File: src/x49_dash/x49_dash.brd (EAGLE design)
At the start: 171.4 x 95.2 mm, 63 parts, among them J1 1-776276-1, Q1 BSS138, U2 MCP2562

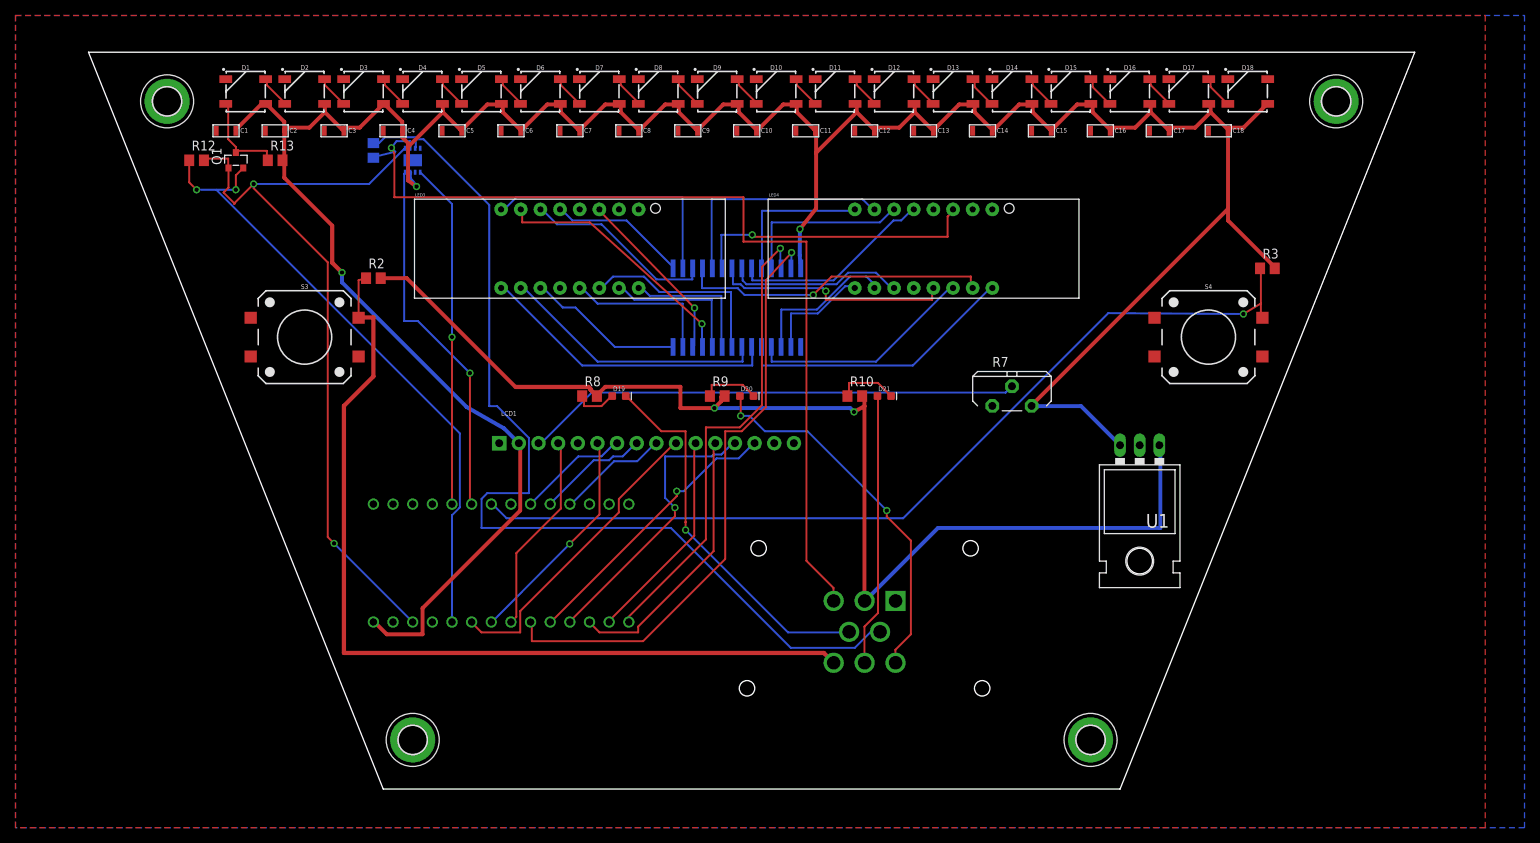
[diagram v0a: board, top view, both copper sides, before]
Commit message: x49_dash: WIP Move teensy parts closer together, clean up routing
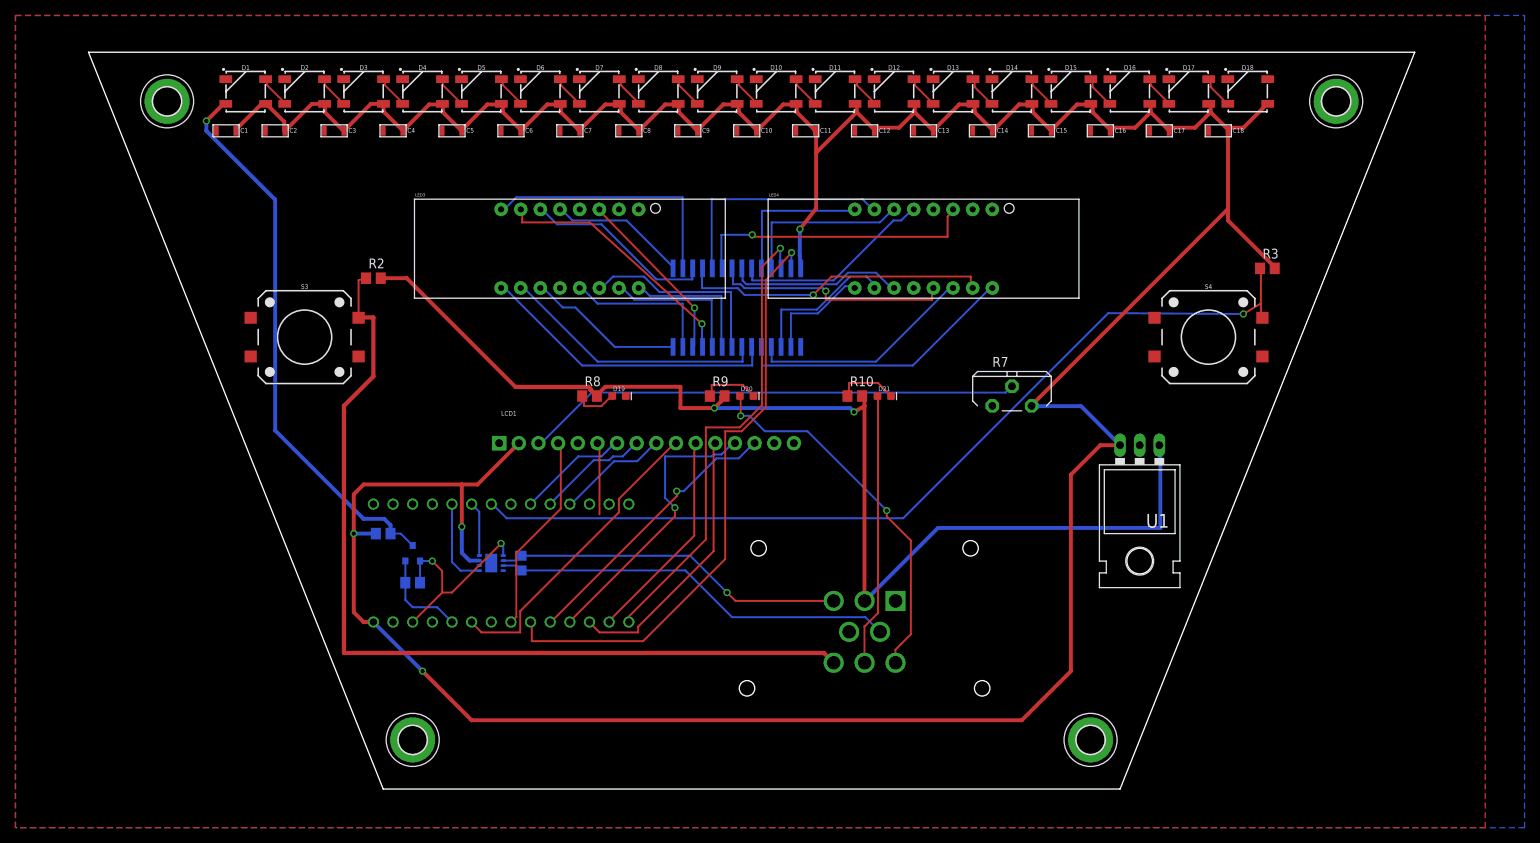
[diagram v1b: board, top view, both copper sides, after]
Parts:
- moved R12 61.3 mm to (6.35, 26.7), flipped to the bottom, turned to 180 degrees
- moved R1 56.6 mm to (20.3, 29.2), turned to 90 degrees
- moved Q1 55.7 mm to (6.35, 30.5), flipped to the bottom
- moved U2 53.1 mm to (16.5, 29.2), turned to 90 degrees
- moved R13 50.2 mm to (2.54, 33.0), flipped to the bottom
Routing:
- net VIN: track 384.3 -> 472.3 mm, vias 3 -> 4
- net CAN_L: track 129.2 -> 52.3 mm
- net CAN_H: track 120.8 -> 45.4 mm
- net 3.3V: track 100.3 -> 26.3 mm
- net LEVEL-SHIFT: track 81.8 -> 12.2 mm, vias 2 -> 0
- net N$52: track 12.1 -> 71.7 mm, vias 0 -> 1
- net ACCEL_LED: track 49.0 -> 0.00 mm, vias 1 -> 0
- net CAN-RX: track 47.6 -> 7.18 mm, vias 1 -> 0
- net CAN-TX: track 44.6 -> 11.5 mm, vias 1 -> 0
- net LCD-E: track 29.0 -> 9.31 mm, vias 1 -> 0

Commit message: x49_dash: WIP total relayout
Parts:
- added R4, R5: 10k, eagle-ltspice:R0805
- added U3: (no value), microbuilder:SOP28_300MIL
- moved J1 54.3 mm to (49.5, 72.4), turned to 180 degrees
- moved R13 36.4 mm to (34.8, 49.8), turned to 270 degrees
- moved Q1 35.8 mm to (38.1, 47.0)
- moved R1 35.8 mm to (52.1, 45.7)
- moved R12 35.8 mm to (38.1, 43.2)
- moved U$1 35.8 mm to (49.5, 45.7)
- moved U2 35.8 mm to (48.3, 45.7)
- moved U5 28.7 mm to (76.2, 55.9), turned to 180 degrees
- moved R3 21.6 mm to (100.3, 53.3), turned to 180 degrees
- moved R2 13.7 mm to (3.81, 52.6)
- moved R7 7.62 mm to (91.4, 50.8)
- moved LED3 3.81 mm to (22.9, 69.8)
- moved LED4 3.81 mm to (76.2, 69.8)
- moved LCD1 1.27 mm to (49.5, 30.5), turned to 180 degrees
- moved R10 0.76 mm to (63.5, 51.6), turned to 90 degrees
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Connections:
- net LEVEL-SHIFT renamed LED_DI_3V3
- net N$52 renamed LED_DI_5V
- net A-2: now also U3.P$25; no longer U5.P$17
- net B-2: now also U3.P$24; no longer U5.P$16
- net C-2: now also U3.P$23; no longer U5.P$15
- net D-2: now also U3.P$22; no longer U5.P$14
- net DIG2-1: now also U3.P$2; no longer U5.P$6
- net DIG2-2: now also U3.P$3; no longer U5.P$7
- net DIG2-3: now also U3.P$4; no longer U5.P$8
- net DIG2-4: now also U3.P$5; no longer U5.P$9
- net DP-2: now also U3.P$18; no longer U5.P$10
- net E-2: now also U3.P$21; no longer U5.P$13
- net F-2: now also U3.P$20; no longer U5.P$12
- net G-2: now also U3.P$19; no longer U5.P$11
- net GND: now also U3.P$1
- net SCK: now also R5.1, U3.P$26
- net SDA: now also R4.1, U3.P$27
- net VIN: now also R4.2, R5.2, U3.P$28
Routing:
- net VIN: track 472.3 -> 279.5 mm, vias 4 -> 3
- net FLEX: track 116.6 -> 9.87 mm
- net VDD12V_DASH: track 154.3 -> 58.8 mm, vias 2 -> 0
- net BUTTON-1: track 118.8 -> 44.4 mm
- net N$27: track 64.2 -> 0.00 mm
- net SDA: track 78.4 -> 22.0 mm, vias 1 -> 0
- net CAN_L: track 52.3 -> 2.52 mm
- net WARM_LED: track 48.4 -> 0.00 mm, vias 2 -> 0
- net CAN_H: track 45.4 -> 2.52 mm, vias 1 -> 0
- net LCD-D3: track 39.8 -> 0.00 mm
- net LCD-D6: track 37.4 -> 0.00 mm, vias 1 -> 0
- net LCD-D7: track 36.4 -> 0.00 mm, vias 1 -> 0
- net LCD-D5: track 35.5 -> 0.00 mm
- net NEUTRAL_LED: track 35.2 -> 0.00 mm
- net DIG2-1: track 39.0 -> 4.60 mm
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
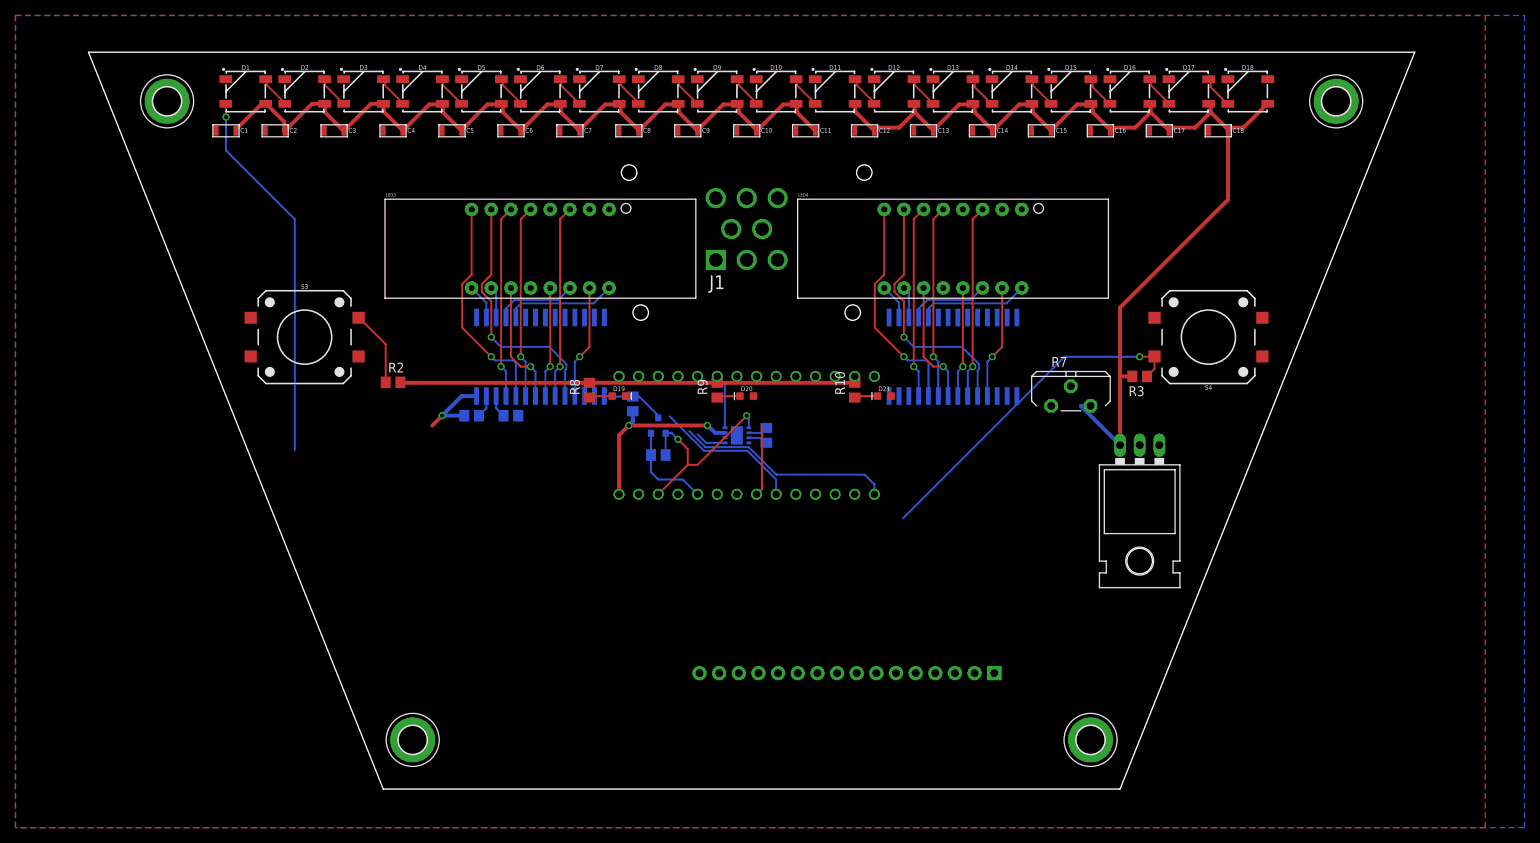
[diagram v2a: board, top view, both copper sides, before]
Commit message: x49_dash: Finish relayout
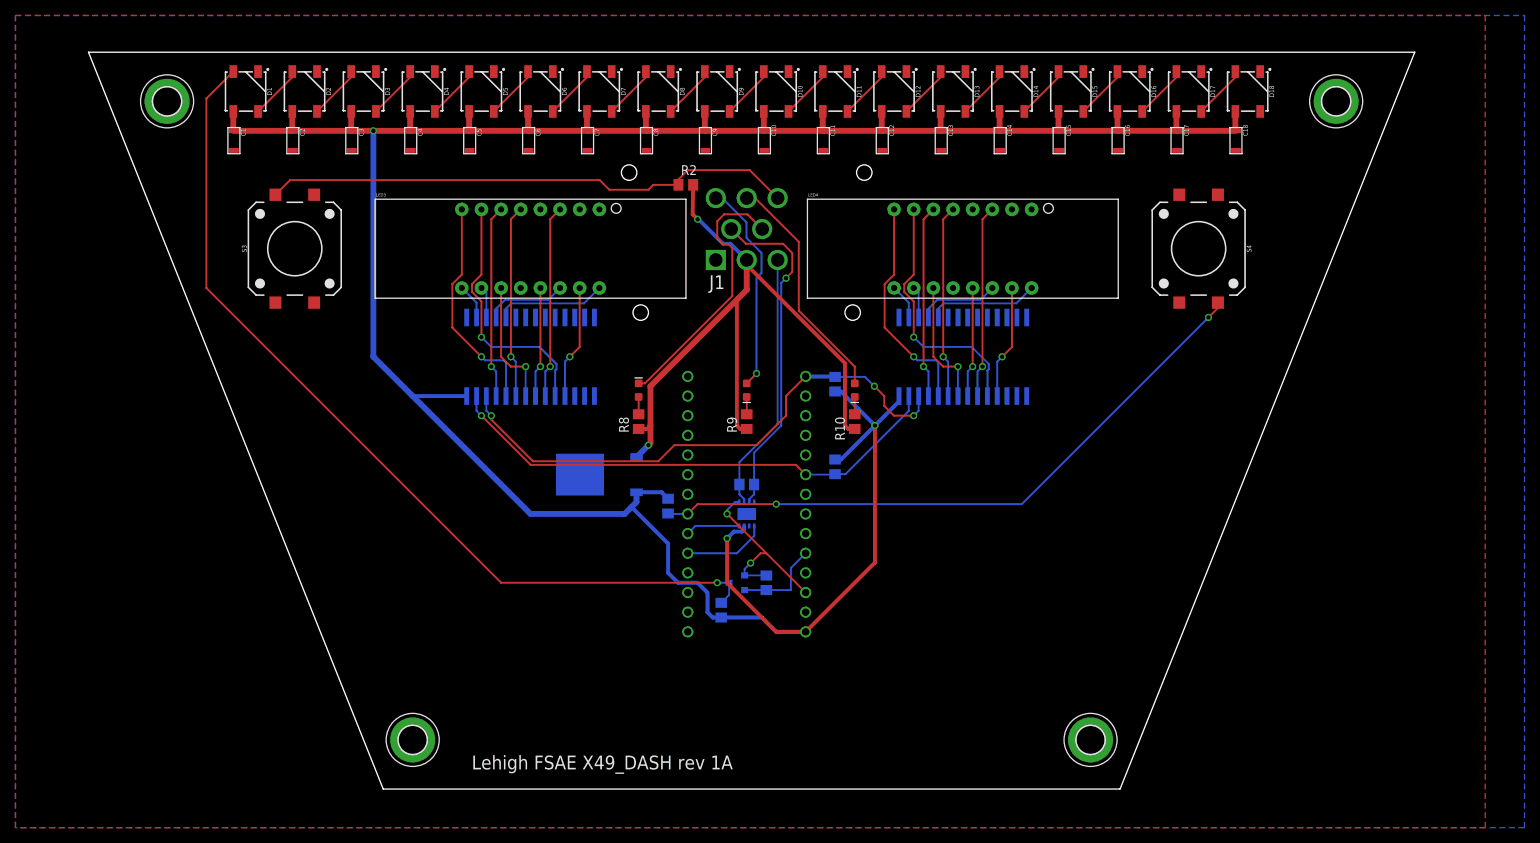
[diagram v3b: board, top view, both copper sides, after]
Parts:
- removed LCD1: LCD-16X2NOHOLES, SparkFun-Displays:LCD-16X2_NOHOLESNOSILK
- removed R7: 10k, rcl:PT-10S
- U1: value (none) -> +12v; device SparkFun-IC-Power:TO-220-ALT -> SparkFun-IC-Power:TO-252
- moved U1 69.8 mm to (30.5, 40.6), flipped to the bottom, turned to 270 degrees
- moved R3 63.2 mm to (39.4, 36.6), flipped to the bottom, turned to 90 degrees
- moved R4 47.5 mm to (61.0, 41.7), turned to 90 degrees
- moved R2 45.7 mm to (41.7, 78.1)
- moved R5 42.1 mm to (61.0, 52.3), turned to 270 degrees
- moved R13 29.0 mm to (46.2, 23.1)
- moved Q1 22.7 mm to (48.3, 26.7), turned to 270 degrees
- moved R12 21.6 mm to (52.1, 26.7), turned to 90 degrees
- moved S3 11.5 mm to (-8.89, 69.8), turned to 90 degrees
- moved S4 11.5 mm to (108.0, 69.8), turned to 270 degrees
- moved U2 10.2 mm to (49.5, 35.6), turned to 0 degrees
- moved U$1 8.89 mm to (49.5, 36.8), turned to 180 degrees
- moved R8 7.54 mm to (35.6, 47.5), turned to 270 degrees
- moved R1 6.84 mm to (49.5, 39.4), turned to 0 degrees
- moved R9 5.57 mm to (49.5, 47.5), turned to 270 degrees
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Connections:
- removed net A: LCD1.15
- removed net K: LCD1.16
- removed net LCD-D0: LCD1.7, U$1.7
- removed net LCD-D1: LCD1.8, U$1.8
- removed net LCD-D2: LCD1.9, U$1.9
- removed net LCD-D3: LCD1.10, U$1.21/A7
- removed net LCD-D4: LCD1.11, U$1.14/A0
- removed net LCD-D5: LCD1.12, U$1.15/A1
- removed net LCD-D6: LCD1.13, U$1.16/A2
- removed net LCD-D7: LCD1.14, U$1.17/A3
- removed net LCD-E: LCD1.6, U$1.20/A6
- removed net LCD-RS: LCD1.4, U$1.19/A5
- removed net N$27: LCD1.3, R7.3
- net GND: now also U1.3; no longer LCD1.1, LCD1.5, R7.1, U1.GND
- net VDD12V_DASH: now also U1.1; no longer U1.IN
- net VIN: now also U1.2; no longer LCD1.2, R7.2, U1.OUT
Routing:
- net VIN: track 279.5 -> 364.1 mm
- net LED_DI_5V: track 55.4 -> 115.8 mm
- net FLEX: track 9.87 -> 69.2 mm
- net SDA: track 22.0 -> 66.5 mm, vias 0 -> 1
- net CAN_L: track 2.52 -> 44.1 mm, vias 0 -> 1
- net SCK: track 31.0 -> 71.8 mm, vias 0 -> 3
- net BUTTON-1: track 44.4 -> 82.8 mm, vias 1 -> 2
- net ACCEL_LED: track 0.00 -> 34.6 mm
- net VDD12V_DASH: track 58.8 -> 92.3 mm, vias 0 -> 2
- net CAN_H: track 2.52 -> 33.6 mm
- net NEUTRAL_LED: track 0.00 -> 30.4 mm
- net WARM_LED: track 0.00 -> 27.7 mm, vias 0 -> 1
- net LCD-RS: track 9.21 -> 0.00 mm
- net CAN-TX: track 3.99 -> 10.8 mm
- net N$13: track 4.23 -> 6.98 mm
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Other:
- board text added: "Lehigh FSAE X49_DASH rev 1A"

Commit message: x49_dash: Rev 1B
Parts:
- added R11, R14, R6, R7: 10k, eagle-ltspice:R0805
- added S1, S2, S5, S6: MOMENTARY-SWITCH-SPST-SMD-12MM, SparkFun-Switches:TACTILE_SWITCH_SMD_12MM
- added U$2: ADAFRUIT-OLED-BREAKOUT, adafruit:OLED-1.27INCH-BREAKOUT
- moved S3 97.2 mm to (80.0, 30.5), turned to 0 degrees
- moved S4 60.2 mm to (80.0, 16.5), turned to 0 degrees
- moved R5 15.1 mm to (61.0, 37.2)
- moved R13 8.53 mm to (39.4, 28.2)
- moved U1 6.84 mm to (24.1, 43.2)
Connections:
- removed net 3.3V: Q1.1, R12.2, U$1.3.3V, U2.P5
- new net 3V3: U$2.9
- new net BUTTON-2: R7.1, S2.3, U$1.21/A7
- new net BUTTON-3: R11.1, S3.3, U$1.22/A8
- new net BUTTON-4: R14.1, S4.3, U$1.23/A9
- new net BUTTON-5: R3.1, S5.3, U$1.5
- new net MISO: U$1.12, U$2.7
- new net MOSI: U$1.11, U$2.1
- new net OLED_CS: U$1.10, U$2.5
- new net OLED_DC: U$1.15/A1, U$2.3
- new net OLED_RESET: U$1.14/A0, U$2.4
- new net SCL: R5.1, U$1.19/A5, U3.P$26, U5.P$26
- new net SDCARD_CD: U$1.8, U$2.8
- new net SDCARD_CS: U$1.9, U$2.6
- new net VDD_3V3: Q1.1, R11.2, R12.2, R14.2, R6.2, R7.2, U$1.3.3V, U2.P5
- net BUTTON-1: now also R6.1, S1.3, U$1.20/A6; no longer R3.1, S4.3, U$1.5
- net FLEX: now also S6.3; no longer S3.3
- net GND: now also S1.1, S2.1, S5.1, S6.1, U$2.11, U$2.P$1, U$2.P$2, U$2.P$3, U$2.P$4
- net LED_DI_3V3: now also U$1.2; no longer U$1.22/A8
- net SCK: now also U$2.2; no longer R5.1, U3.P$26, U5.P$26
- net VIN: now also U$2.10
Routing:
- net BUTTON-5: track 0.00 -> 83.9 mm, vias 0 -> 2
- net OLED_RESET: track 0.00 -> 55.5 mm, vias 0 -> 2
- net SCL: track 0.00 -> 54.3 mm, vias 0 -> 1
- net OLED_DC: track 0.00 -> 53.5 mm, vias 0 -> 4
- net OLED_CS: track 0.00 -> 53.5 mm, vias 0 -> 5
- net MISO: track 0.00 -> 51.2 mm, vias 0 -> 1
- net MOSI: track 0.00 -> 49.8 mm, vias 0 -> 2
- net SDCARD_CD: track 0.00 -> 45.1 mm, vias 0 -> 2
- net BUTTON-1: track 82.8 -> 38.3 mm, vias 2 -> 0
- net BUTTON-2: track 0.00 -> 44.5 mm
- net SDCARD_CS: track 0.00 -> 42.7 mm, vias 0 -> 1
- net BUTTON-4: track 0.00 -> 36.9 mm, vias 0 -> 1
- net BUTTON-3: track 0.00 -> 34.2 mm, vias 0 -> 1
- net VDD_3V3: track 0.00 -> 31.5 mm, vias 0 -> 2
- net 3.3V: track 24.2 -> 0.00 mm, vias 2 -> 0
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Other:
- board text added: "Lehigh FSAE X49_DASH rev 1B"
- board text removed: "Lehigh FSAE X49_DASH rev 1A"

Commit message: x49_dash: Rev 1C
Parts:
- moved R13 4.32 mm to (39.4, 32.5), turned to 90 degrees
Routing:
- net SCL: track 54.3 -> 72.4 mm
- net VIN: track 374.7 -> 361.2 mm
- net OLED_CS: track 53.5 -> 50.7 mm
- net LED_DI_5V: track 118.5 -> 119.5 mm
- net OLED_DC: track 53.5 -> 54.2 mm, vias 4 -> 2
- net CAN-RX: track 7.18 -> 7.06 mm, vias 0 -> 1
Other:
- board text added: "* Made in Mohler by Pixies *"
- board text added: "Lehigh FSAE X49_DASH rev 1C"
- board text removed: "Lehigh FSAE X49_DASH rev 1B"
